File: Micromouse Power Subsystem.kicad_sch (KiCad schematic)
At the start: 3 parts, among them J2 Conn_02x16_Odd_Even, U1 INA219AxD

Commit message: Created branch for Josh
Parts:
- R1: footprint (none) -> Resistor_SMD:R_Shunt_Ohmite_LVK12
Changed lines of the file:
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@@
       (effects (font (size 1.27 1.27)) (justify right))
     )
-    (property "Footprint" "" (at 45.974 92.456 90)
+    (property "Footprint" "Resistor_SMD:R_Shunt_Ohmite_LVK12" (at 45.974 92.456 90)
       (effects (font (size 1.27 1.27)) hide)
     )

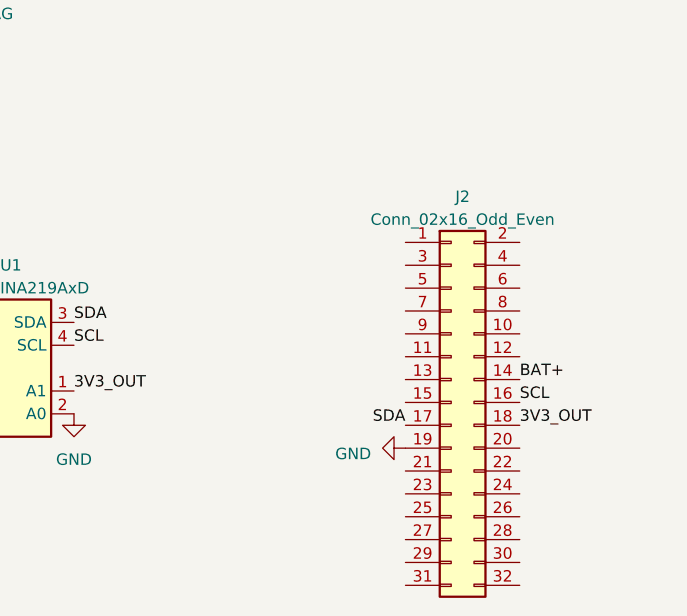
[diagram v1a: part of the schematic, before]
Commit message: Added all net labels for the 32 pin header
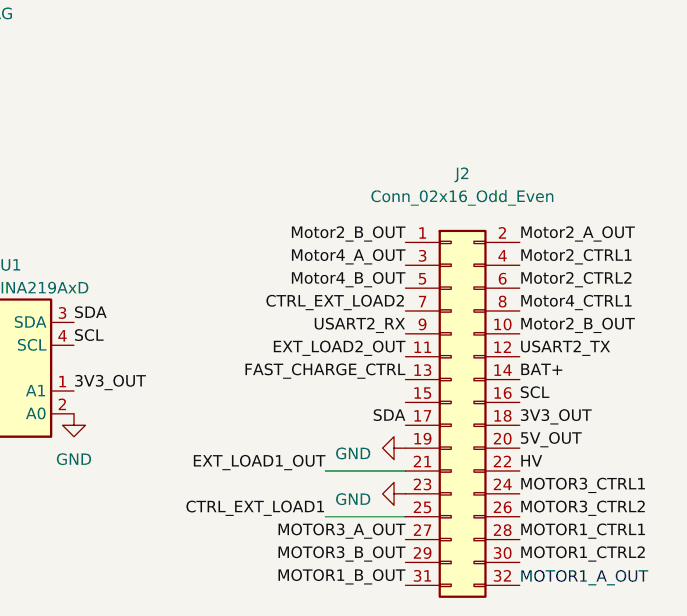
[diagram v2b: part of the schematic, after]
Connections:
- net GND: now also J2.23 (Pin_23)
- net Motor2_B_OUT: now reaches J2.1 (Pin_1)
- net Motor2_B_OUT: now also J2.10 (Pin_10)
- net EXT_LOAD2_OUT: now reaches J2.11 (Pin_11)
- net USART2_TX: now reaches J2.12 (Pin_12)
- net FAST_CHARGE_CTRL: now reaches J2.13 (Pin_13)
- net Motor2_A_OUT: now reaches J2.2 (Pin_2)
- net 5V_OUT: now reaches J2.20 (Pin_20)
- net EXT_LOAD1_OUT: now reaches J2.21 (Pin_21)
- net HV: now reaches J2.22 (Pin_22)
- net MOTOR3_CTRL1: now reaches J2.24 (Pin_24)
- net CTRL_EXT_LOAD1: now reaches J2.25 (Pin_25)
- net MOTOR3_CTRL2: now reaches J2.26 (Pin_26)
- net MOTOR3_A_OUT: now reaches J2.27 (Pin_27)
- net MOTOR1_CTRL1: now reaches J2.28 (Pin_28)
- net MOTOR3_B_OUT: now reaches J2.29 (Pin_29)
- net Motor4_A_OUT: now reaches J2.3 (Pin_3)
- net MOTOR1_CTRL2: now reaches J2.30 (Pin_30)
- net MOTOR1_B_OUT: now reaches J2.31 (Pin_31)
- net Motor2_CTRL1: now reaches J2.4 (Pin_4)
- net Motor4_B_OUT: now reaches J2.5 (Pin_5)
- net Motor2_CTRL2: now reaches J2.6 (Pin_6)
- net CTRL_EXT_LOAD2: now reaches J2.7 (Pin_7)
- net Motor4_CTRL1: now reaches J2.8 (Pin_8)
- net USART2_RX: now reaches J2.9 (Pin_9)
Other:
- note added: "MOTOR1_A_OUT"
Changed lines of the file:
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@@
+    (stroke (width 0) (type default))
+  )
+  (wire (pts (xy 107.95 110.49) (xy 116.84 110.49))
     (stroke (width 0) (type default))
   )
@@
     (stroke (width 0) (type default))
   )
+  (wire (pts (xy 107.95 105.41) (xy 116.84 105.41))
+    (stroke (width 0) (type default))
+  )
   (wire (pts (xy 46.99 96.52) (xy 46.99 100.33))
     (stroke (width 0) (type default))
@@
     (stroke (width 0) (type default))
   )
+  (text "MOTOR1_A_OUT" (at 129.54 118.11 0)
+    (effects (font (size 1.27 1.27)) (justify left bottom))
+  )
   (label "3V3_OUT" (at 69.85 83.82 90) (fields_autoplaced)
     (effects (font (size 1.27 1.27)) (justify left bottom))
   )
+  (label "CTRL_EXT_LOAD2" (at 116.84 87.63 180) (fields_autoplaced)
+    (effects (font (size 1.27 1.27)) (justify right bottom))
+  )
+  (label "USART2_TX" (at 129.54 92.71 0) (fields_autoplaced)
+    (effects (font (size 1.27 1.27)) (justify left bottom))
+  )
+  (label "EXT_LOAD1_OUT" (at 107.95 105.41 180) (fields_autoplaced)
+    (effects (font (size 1.27 1.27)) (justify right bottom))
+  )
+  (label "MOTOR3_CTRL2" (at 129.54 110.49 0) (fields_autoplaced)
+    (effects (font (size 1.27 1.27)) (justify left bottom))
+  )
+  (label "EXT_LOAD2_OUT" (at 116.84 92.71 180) (fields_autoplaced)
+    (effects (font (size 1.27 1.27)) (justify right bottom))
+  )
+  (label "MOTOR1_CTRL1" (at 129.54 113.03 0) (fields_autoplaced)
+    (effects (font (size 1.27 1.27)) (justify left bottom))
+  )
+  (label "Motor2_CTRL1" (at 129.54 82.55 0) (fields_autoplaced)
+    (effects (font (size 1.27 1.27)) (justify left bottom))
+  )
+  (label "Motor4_A_OUT" (at 116.84 82.55 180) (fields_autoplaced)
+    (effects (font (size 1.27 1.27)) (justify right bottom))
+  )
+  (label "MOTOR3_CTRL1" (at 129.54 107.95 0) (fields_autoplaced)
+    (effects (font (size 1.27 1.27)) (justify left bottom))
+  )
+  (label "Motor2_A_OUT" (at 129.54 80.01 0) (fields_autoplaced)
+    (effects (font (size 1.27 1.27)) (justify left bottom))
+  )
+  (label "Motor2_CTRL2" (at 129.54 85.09 0) (fields_autoplaced)
+    (effects (font (size 1.27 1.27)) (justify left bottom))
+  )
   (label "V_Switch" (at 46.99 83.82 0) (fields_autoplaced)
     (effects (font (size 1.27 1.27)) (justify left bottom))
   )
+  (label "Motor4_CTRL1" (at 129.54 87.63 0) (fields_autoplaced)
+    (effects (font (size 1.27 1.27)) (justify left bottom))
+  )
+  (label "HV" (at 129.54 105.41 0) (fields_autoplaced)
+    (effects (font (size 1.27 1.27)) (justify left bottom))
+  )
+  (label "Motor2_B_OUT" (at 129.54 90.17 0) (fields_autoplaced)
+    (effects (font (size 1.27 1.27)) (justify left bottom))
+  )
   (label "3V3_OUT" (at 129.54 100.33 0) (fields_autoplaced)
     (effects (font (size 1.27 1.27)) (justify left bottom))
   )
+  (label "Motor4_B_OUT" (at 116.84 85.09 180) (fields_autoplaced)
+    (effects (font (size 1.27 1.27)) (justify right bottom))
+  )
+  (label "FAST_CHARGE_CTRL" (at 116.84 95.25 180) (fields_autoplaced)
+    (effects (font (size 1.27 1.27)) (justify right bottom))
+  )
+  (label "5V_OUT" (at 129.54 102.87 0) (fields_autoplaced)
+    (effects (font (size 1.27 1.27)) (justify left bottom))
+  )
+  (label "MOTOR1_CTRL2" (at 129.54 115.57 0) (fields_autoplaced)
+    (effects (font (size 1.27 1.27)) (justify left bottom))
+  )
   (label "SCL" (at 129.54 97.79 0) (fields_autoplaced)
     (effects (font (size 1.27 1.27)) (justify left bottom))
   )
+  (label "Motor2_B_OUT" (at 116.84 80.01 180) (fields_autoplaced)
+    (effects (font (size 1.27 1.27)) (justify right bottom))
+  )
+  (label "CTRL_EXT_LOAD1" (at 107.95 110.49 180) (fields_autoplaced)
+    (effects (font (size 1.27 1.27)) (justify right bottom))
+  )
   (label "BAT+" (at 129.54 95.25 0) (fields_autoplaced)
     (effects (font (size 1.27 1.27)) (justify left bottom))
   )
+  (label "MOTOR3_A_OUT" (at 116.84 113.03 180) (fields_autoplaced)
+    (effects (font (size 1.27 1.27)) (justify right bottom))
+  )
+  (label "USART2_RX" (at 116.84 90.17 180) (fields_autoplaced)
+    (effects (font (size 1.27 1.27)) (justify right bottom))
+  )
   (label "3V3_OUT" (at 80.01 96.52 0) (fields_autoplaced)
     (effects (font (size 1.27 1.27)) (justify left bottom))
@@
   (label "SCL" (at 80.01 91.44 0) (fields_autoplaced)
     (effects (font (size 1.27 1.27)) (justify left bottom))
+  )
+  (label "MOTOR3_B_OUT" (at 116.84 115.57 180) (fields_autoplaced)
+    (effects (font (size 1.27 1.27)) (justify right bottom))
+  )
+  (label "MOTOR1_B_OUT" (at 116.84 118.11 180) (fields_autoplaced)
+    (effects (font (size 1.27 1.27)) (justify right bottom))
   )
   (label "SDA" (at 116.84 100.33 180) (fields_autoplaced)
@@
     )
   )
+  (symbol (lib_id "power:GND") (at 116.84 107.95 270) (unit 1)
+    (in_bom yes) (on_board yes) (dnp no) (fields_autoplaced)
+    (property "Reference" "#PWR06" (at 110.49 107.95 0)
+      (effects (font (size 1.27 1.27)) hide)
+    )
+    (property "Value" "GND" (at 113.03 108.585 90)
+      (effects (font (size 1.27 1.27)) (justify right))
+    )
+    (property "Footprint" "" (at 116.84 107.95 0)
+      (effects (font (size 1.27 1.27)) hide)
+    )
+    (property "Datasheet" "" (at 116.84 107.95 0)
+      (effects (font (size 1.27 1.27)) hide)
+    )
+    (pin "1")
+    (instances
+      (project "Micromouse Power Subsystem"
+        (path "/c31c9b5f-16c8-4039-9f8b-b05613c282c9"
+          (reference "#PWR06") (unit 1)
+        )
+      )
+    )
+  )
   (symbol (lib_id "Connector_Generic:Conn_02x16_Odd_Even") (at 121.92 97.79 0) (unit 1)
-    (in_bom yes) (on_board yes) (dnp no) (fields_autoplaced)
-    (property "Reference" "J2" (at 123.19 74.93 0)
+    (in_bom yes) (on_board yes) (dnp no)
+    (property "Reference" "J2" (at 123.19 72.39 0)
       (effects (font (size 1.27 1.27)))
     )
-    (property "Value" "Conn_02x16_Odd_Even" (at 123.19 77.47 0)
+    (property "Value" "Conn_02x16_Odd_Even" (at 123.19 74.93 0)
       (effects (font (size 1.27 1.27)))
     )

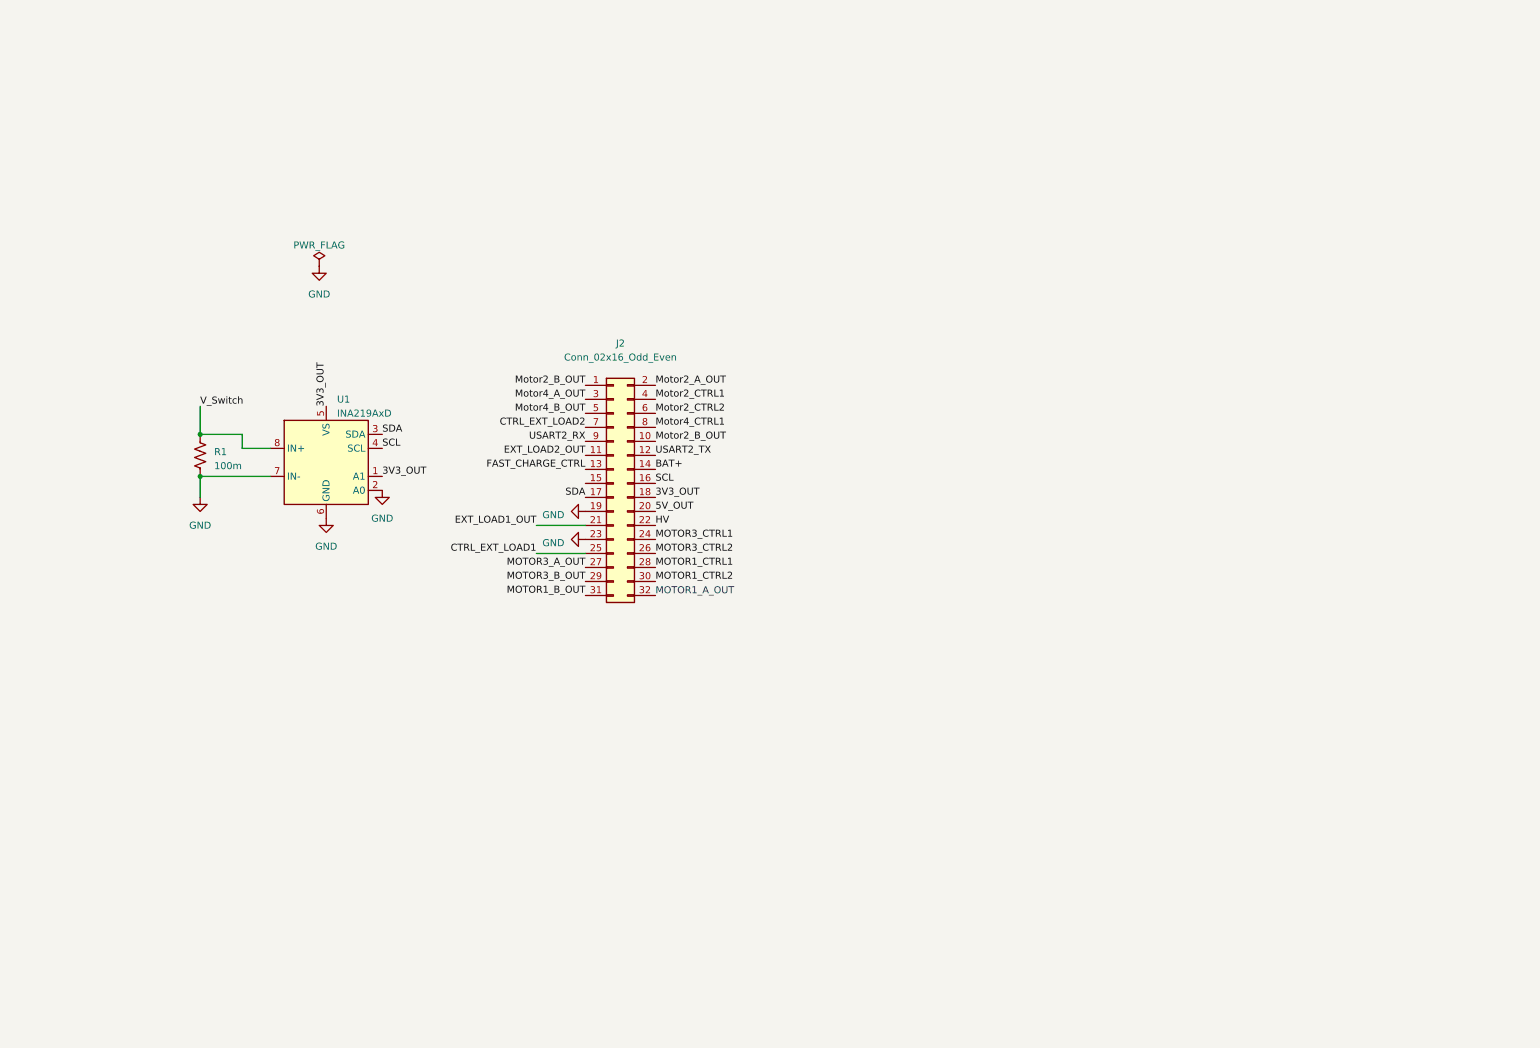
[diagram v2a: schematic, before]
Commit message: Finished the USB-C integration with PD (9V)
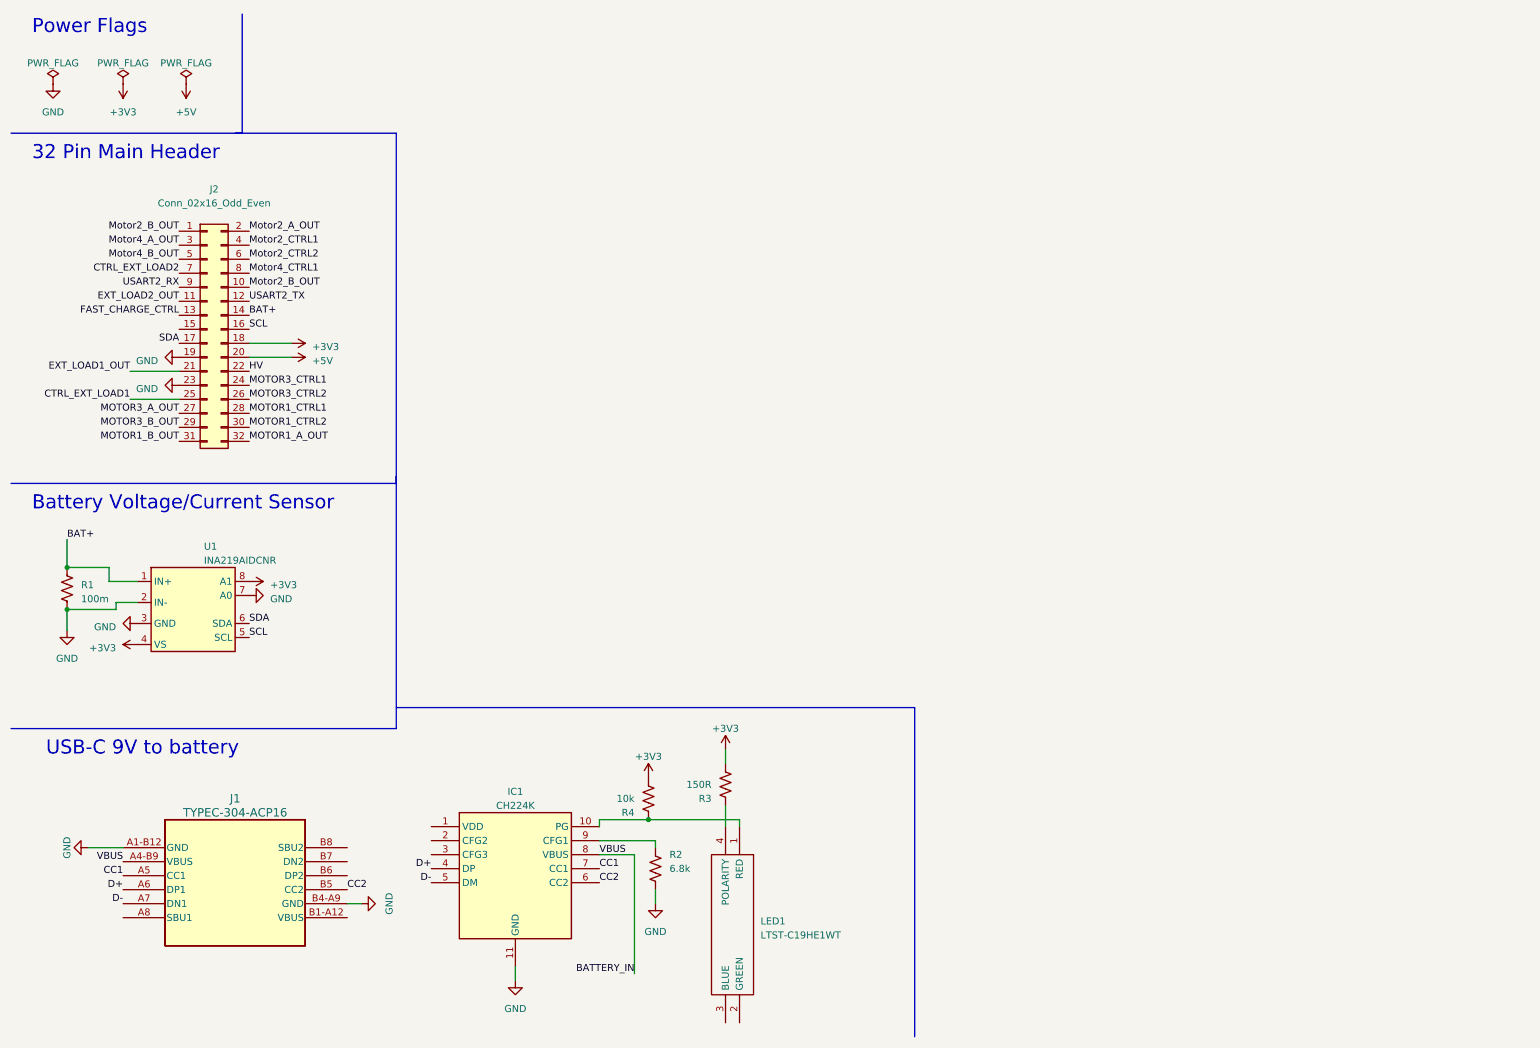
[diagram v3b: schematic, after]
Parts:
- added IC1: CH224K, Components:SOP100P600X180-11N, symbol CH224K:CH224K
- added J1: TYPEC-304-ACP16, Components:TYPEC-304-ACP16_XNP, symbol 2025-03-21_13-44-01:TYPEC-304-ACP16
- added LED1: LTST-C19HE1WT, RGB LED:LTST-C19HE1WT, symbol LTST-C19HE1WT:LTST-C19HE1WT
- added R2: 6.8k, Resistor_THT:R_Axial_DIN0204_L3.6mm_D1.6mm_P1.90mm_Vertical, symbol Device:R_US
- added R3: 150R, Resistor_THT:R_Axial_DIN0204_L3.6mm_D1.6mm_P1.90mm_Vertical, symbol Device:R_US
- added R4: 10k, Resistor_THT:R_Axial_DIN0204_L3.6mm_D1.6mm_P1.90mm_Vertical, symbol Device:R_US
- R1: LCSC (none) -> C2903476
- U1: value INA219AxD -> INA219AIDCNR; LCSC (none) -> C87469
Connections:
- net BAT+: now also R1.2, U1.1 (IN+)
- net GND: now also U1.3 (GND), IC1.11 (GND), J1.A1-B12 (GND), J1.B4-A9 (GND), R2.1; no longer U1.6 (GND)
- net SCL: now also U1.5 (SCL); no longer U1.4 (SCL)
- net SDA: now also U1.6 (SDA); no longer U1.3 (SDA)
- net MOTOR1_A_OUT: now reaches J2.32 (Pin_32)
- removed net 3V3_OUT: J2.18 (Pin_18), U1.1 (A1), U1.5 (VS)
- net 5V_OUT renamed +5V
- net V_Switch renamed +3V3
- net +3V3: now also J2.18 (Pin_18), U1.4 (VS), R3.1, R4.1; no longer R1.2
- new net: IC1.9 (CFG1), R2.2
- new net: IC1.10 (PG), LED1.1 (RED), R4.2
- new net: LED1.4 (POLARITY), R3.2
- new net BATTERY_IN: IC1.8 (VBUS), J1.A4-B9 (VBUS)
- new net CC1: IC1.7 (CC1), J1.A5 (CC1)
- new net CC2: IC1.6 (CC2), J1.B5 (CC2)
- new net D+: IC1.4 (DP), J1.A6 (DP1)
- new net D-: IC1.5 (DM), J1.A7 (DN1)
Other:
- note added: "32 Pin Main Header"
- note added: "Battery Voltage/Current Sensor"
- note added: "Power Flags"
- note added: "USB-C 9V to battery"
- note removed: "MOTOR1_A_OUT"
- moved on the sheet: J2, R1, U1
